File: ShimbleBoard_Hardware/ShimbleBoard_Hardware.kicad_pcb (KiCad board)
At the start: 2 copper layers, 13 parts, among them U1 TM4C129E_Launchpad, U2 OKI

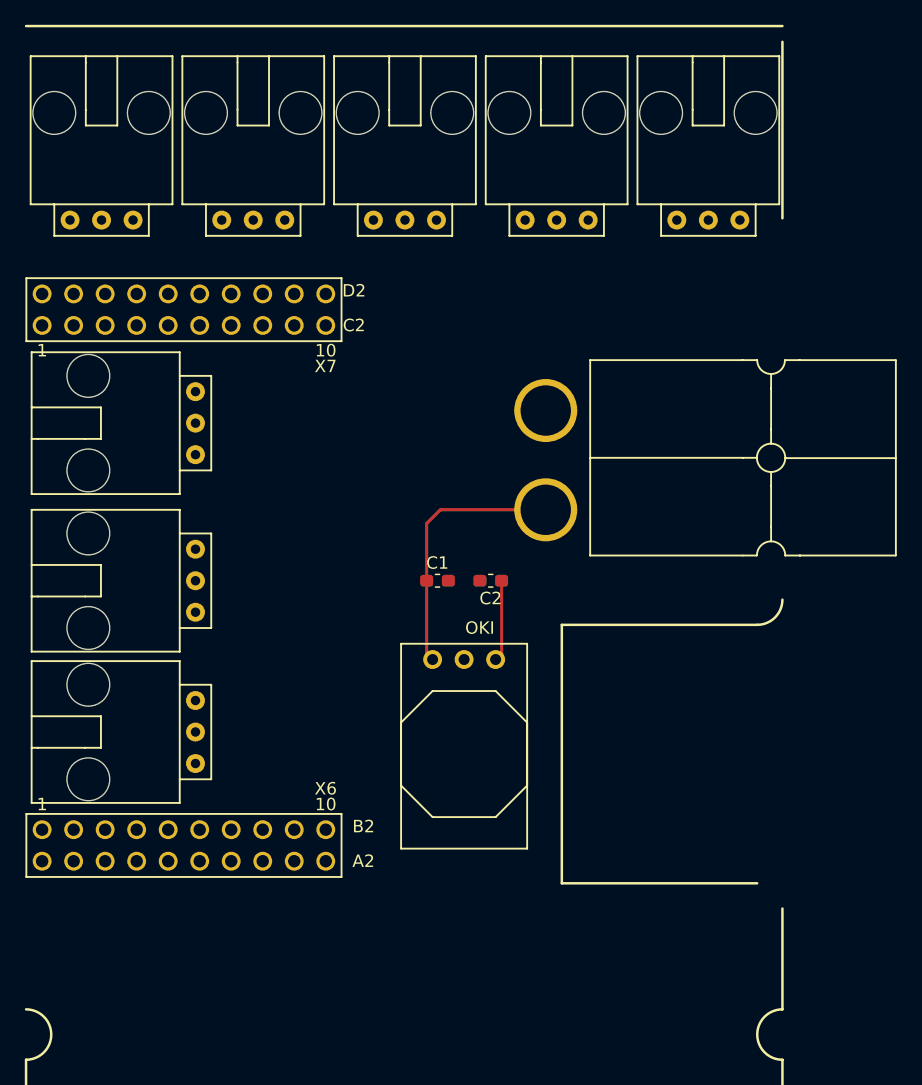
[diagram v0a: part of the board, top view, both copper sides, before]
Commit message: Removed Servo 8 & Increased Power Track Width
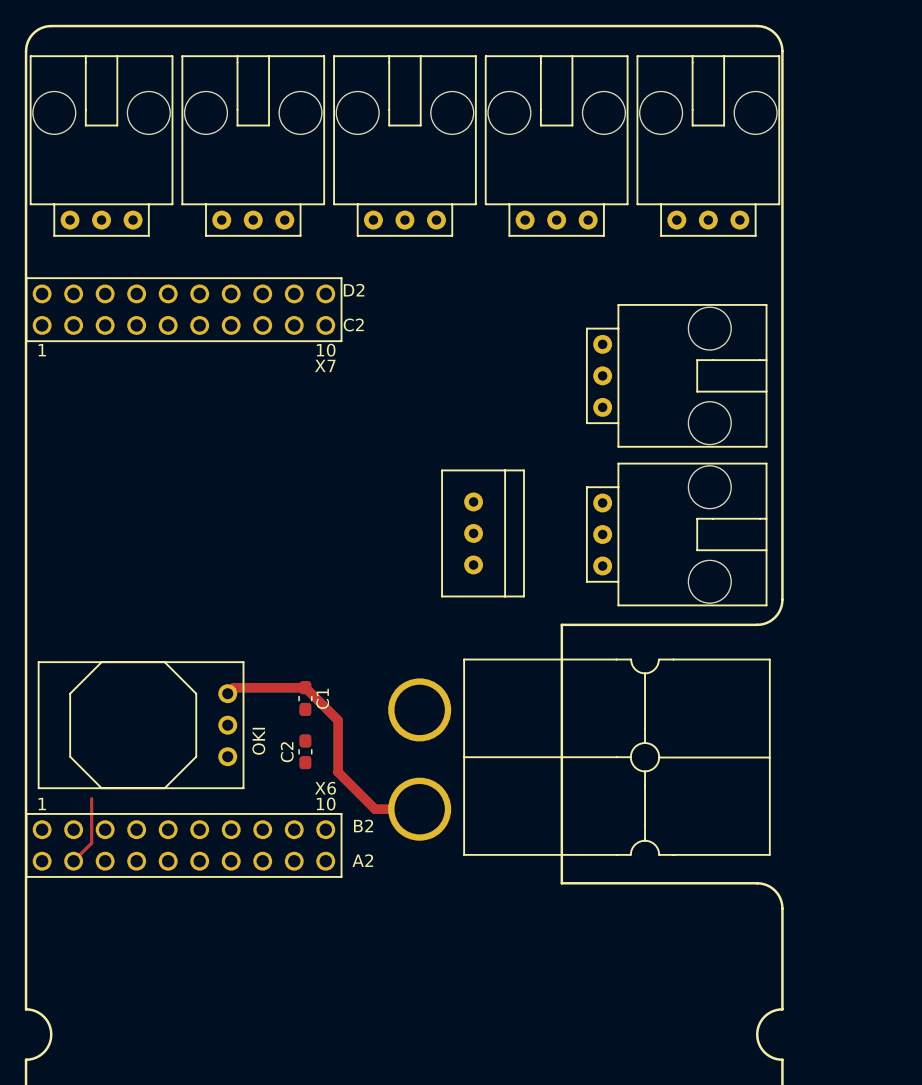
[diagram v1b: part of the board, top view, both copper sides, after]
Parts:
- Conn9: footprint MRDT_Connectors:MOLEX_SL_03_Horizontal -> MRDT_Connectors:MOLEX_SL_03_Vertical
- moved Conn7 43.6 mm to (139.4, 87.6), turned to 270 degrees
- moved Conn8 33.0 mm to (139.4, 100.4), turned to 270 degrees
- moved Conn1 26.2 mm to (128.3, 110.5)
- moved Conn9 25.2 mm to (131.6, 95.2), turned to 270 degrees
- moved C2 20.3 mm to (115.5, 117.9), turned to 90 degrees
- moved C1 14.3 mm to (115.5, 113.6), turned to 270 degrees
- moved U2 12.8 mm to (110.5, 110.7), turned to 270 degrees
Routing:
- net +5V: track 6.55 -> 0.00 mm
- net Servo_6_Ctrl: track 0.00 -> 5.63 mm
- net Net-(C1-Pad1): track 21.2 -> 22.2 mm

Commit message: Board Review
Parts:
- added G***: LOGO, MRDT_Silkscreens:MRDT_Logo_20mm, F.Cu at (105.9, 140.2)
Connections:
- U1 pad PA4: Servo_7_Ctrl -> Net-(U1-PadPA4)
- U1 pad PA5: Servo_8_Ctrl -> Net-(U1-PadPA5)
- U1 pad PA7: Net-(U1-PadPA7) -> Servo_2_Ctrl
- U1 pad PD2: Servo_6_Ctrl -> Net-(U1-PadPD2)
- U1 pad PG1: Servo_1_Ctrl -> Servo_8_Ctrl
- U1 pad PK4: Servo_2_Ctrl -> Servo_7_Ctrl
- U1 pad PK5: Servo_3_Ctrl -> Servo_6_Ctrl
- U1 pad PM0: Servo_4_Ctrl -> Servo_5_Ctrl
- U1 pad PM1: Net-(U1-PadPM1) -> Servo_4_Ctrl
- U1 pad PM6: Net-(U1-PadPM6) -> Servo_3_Ctrl
- U1 pad PM7: Servo_5_Ctrl -> Servo_1_Ctrl
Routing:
- net Servo_7_Ctrl: track 0.00 -> 58.3 mm
- net Servo_5_Ctrl: track 0.00 -> 57.9 mm
- net Servo_8_Ctrl: track 0.00 -> 50.7 mm
- net Servo_4_Ctrl: track 0.00 -> 42.1 mm
- net Servo_6_Ctrl: track 5.63 -> 43.1 mm
- net Servo_2_Ctrl: track 0.00 -> 14.9 mm
- net Servo_3_Ctrl: track 0.00 -> 12.3 mm
- net Servo_1_Ctrl: track 0.00 -> 7.78 mm
- net +5V: track 0.00 -> 6.46 mm
- added copper zone on B.Cu, net +5V
- added copper zone on F.Cu, net GND
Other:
- board text added: "ShimbleBoard_Hardware, Rev. 1 Mars Rover Design Team, 2019 Missouri S&T Andrew Phillips"

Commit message: Revised Schematic
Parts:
- added C3: 10uF, Capacitor_SMD:C_0603_1608Metric_Pad1.05x0.95mm_HandSolder, F.Cu at (61.3, 88.9)
- added C4: 10uF, Capacitor_SMD:C_0603_1608Metric_Pad1.05x0.95mm_HandSolder, F.Cu at (38.2, 98.8)
- added D1: D_Schottky, Diode_SMD:D_0603_1608Metric_Pad1.05x0.95mm_HandSolder, F.Cu at (60.5, 71.4)
- added D10: Ctrl_6_LED, Diode_SMD:D_0603_1608Metric_Pad1.05x0.95mm_HandSolder, F.Cu at (77.2, 172.7)
- added D11: Ctrl_7_LED, Diode_SMD:D_0603_1608Metric_Pad1.05x0.95mm_HandSolder, F.Cu at (77.2, 177.0)
- added D12: Ctrl_8_LED, Diode_SMD:D_0603_1608Metric_Pad1.05x0.95mm_HandSolder, F.Cu at (77.2, 181.4)
- added D2: D_Schottky, Diode_SMD:D_0603_1608Metric_Pad1.05x0.95mm_HandSolder, F.Cu at (38.2, 88.1)
- added D3: 5V_Act_LED, Diode_SMD:D_0603_1608Metric_Pad1.05x0.95mm_HandSolder, F.Cu at (77.6, 142.2)
- added D4: 5V_Log_LED, Diode_SMD:D_0603_1608Metric_Pad1.05x0.95mm_HandSolder, F.Cu at (77.6, 146.6)
- added D5: Ctrl_1_LED, Diode_SMD:D_0603_1608Metric_Pad1.05x0.95mm_HandSolder, F.Cu at (77.6, 150.9)
- added D6: Ctrl_2_LED, Diode_SMD:D_0603_1608Metric_Pad1.05x0.95mm_HandSolder, F.Cu at (77.6, 155.4)
- added D7: Ctrl_3_LED, Diode_SMD:D_0603_1608Metric_Pad1.05x0.95mm_HandSolder, F.Cu at (92.6, 159.5)
- added D8: Ctrl_4_LED, Diode_SMD:D_0603_1608Metric_Pad1.05x0.95mm_HandSolder, F.Cu at (77.4, 164.1)
- added D9: Ctrl_5_LED, Diode_SMD:D_0603_1608Metric_Pad1.05x0.95mm_HandSolder, F.Cu at (96.2, 166.1)
- added L1: 47uH, Inductor_SMD:L_0603_1608Metric_Pad1.05x0.95mm_HandSolder, F.Cu at (57.8, 78.0)
- added L2: 47uH, Diode_SMD:D_0603_1608Metric_Pad1.05x0.95mm_HandSolder, F.Cu at (37.3, 93.5)
- added R1: 500, Resistor_SMD:R_0603_1608Metric_Pad1.05x0.95mm_HandSolder, F.Cu at (72.0, 142.2)
- added R10: 500, Resistor_SMD:R_0603_1608Metric_Pad1.05x0.95mm_HandSolder, F.Cu at (72.0, 181.4)
- added R2: 500, Resistor_SMD:R_0603_1608Metric_Pad1.05x0.95mm_HandSolder, F.Cu at (72.0, 146.6)
- added R3: 500, Resistor_SMD:R_0603_1608Metric_Pad1.05x0.95mm_HandSolder, F.Cu at (72.0, 150.9)
- added R4: 500, Resistor_SMD:R_0603_1608Metric_Pad1.05x0.95mm_HandSolder, F.Cu at (72.0, 155.4)
- added R5: 500, Resistor_SMD:R_0603_1608Metric_Pad1.05x0.95mm_HandSolder, F.Cu at (72.0, 159.8)
- added R6: 500, Resistor_SMD:R_0603_1608Metric_Pad1.05x0.95mm_HandSolder, F.Cu at (72.0, 164.1)
- added R7: 500, Resistor_SMD:R_0603_1608Metric_Pad1.05x0.95mm_HandSolder, F.Cu at (72.0, 168.4)
- added R8: 500, Resistor_SMD:R_0603_1608Metric_Pad1.05x0.95mm_HandSolder, F.Cu at (72.0, 172.7)
- added R9: 500, Resistor_SMD:R_0603_1608Metric_Pad1.05x0.95mm_HandSolder, F.Cu at (72.0, 177.0)
- added U3: AP1059, Package_SO:SOIC-8_3.9x4.9mm_P1.27mm, F.Cu at (45.7, 93.5)
- Conn1: footprint MRDT_Connectors:Anderson_2_Horisontal_Side_by_Side -> MRDT_Connectors:Anderson_3_Horisontal_Side_by_Side
- U2: value OKI -> AP1059; footprint MRDT_Devices:OKI_Horizontal -> Package_SO:SOIC-8_3.9x4.9mm_P1.27mm
- moved U2 53.1 mm to (68.1, 78.7), turned to 0 degrees
- moved Conn9 48.6 mm to (176.8, 77.5)
- moved Conn1 5.43 mm to (129.3, 105.2)
- moved Conn8 2.84 mm to (140.7, 97.9)
- moved Conn7 2.84 mm to (140.7, 85.1)
- moved C2 2.76 mm to (114.0, 115.6), turned to 0 degrees
- moved C1 2.51 mm to (117.4, 112.0), turned to 0 degrees
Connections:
- net Net-(C1-Pad1) renamed V+Log
- C2 pad 1: +5V -> GND
- C2 pad 2: GND -> V+Act
- Conn2 pad 1: +5V -> +5VA
- Conn3 pad 1: +5V -> +5VA
- Conn4 pad 1: +5V -> +5VA
- Conn5 pad 1: +5V -> +5VA
- Conn6 pad 1: +5V -> +5VA
- Conn7 pad 1: +5V -> +5VA
- Conn8 pad 1: +5V -> +5VA
- Conn9 pad 1: +5V -> +5VA
- U1 pad +5V: +5V -> +5VL
- U2 pad 2: GND -> Net-(D1-Pad1)
- U2 pad 3: +5V -> +5VL
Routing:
- net Servo_5_Ctrl: track 57.9 -> 0.00 mm
- net Servo_7_Ctrl: track 58.3 -> 24.7 mm
- net Servo_8_Ctrl: track 50.7 -> 27.8 mm
- net V+Log: track 22.2 -> 0.00 mm
- net Servo_6_Ctrl: track 43.1 -> 21.6 mm
- net +5V: track 6.46 -> 0.00 mm
- added copper zone on B.Cu, net +5VL
- removed copper zone on B.Cu, net +5V

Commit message: Work hours 2018-11-17
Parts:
- moved D12 87.2 mm to (114.3, 102.5)
- moved R10 87.2 mm to (109.1, 102.5)
- moved D11 86.0 mm to (114.3, 99.4)
- moved R9 86.0 mm to (109.1, 99.4)
- moved D10 84.9 mm to (114.3, 96.4)
- moved R8 84.9 mm to (109.1, 96.4)
- moved R7 83.9 mm to (109.1, 93.1)
- moved D9 75.2 mm to (114.3, 93.1)
- moved D1 73.5 mm to (115.2, 120.4), turned to 180 degrees
- moved L1 70.5 mm to (116.9, 116.4), turned to 180 degrees
- moved R5 67.0 mm to (98.9, 98.4)
- moved D8 66.9 mm to (104.0, 102.7)
- moved R6 66.9 mm to (98.7, 102.7)
- moved R4 65.7 mm to (98.9, 95.5)
- moved D6 65.5 mm to (104.0, 95.5)
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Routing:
- net Servo_5_Ctrl: track 0.00 -> 57.7 mm
- net GND: track 0.00 -> 56.8 mm
- net +5VL: track 0.00 -> 39.6 mm
- net V+Act: track 0.00 -> 38.5 mm, vias 0 -> 2
- net Servo_7_Ctrl: track 24.7 -> 56.4 mm
- net Servo_6_Ctrl: track 21.6 -> 44.6 mm
- net Servo_8_Ctrl: track 27.8 -> 49.9 mm
- net V+Log: track 0.00 -> 14.9 mm, vias 0 -> 2
- net +5VA: track 0.00 -> 11.1 mm
- net Servo_3_Ctrl: track 12.3 -> 22.5 mm
- net Servo_2_Ctrl: track 14.9 -> 22.0 mm
- net Net-(D1-Pad1): track 0.00 -> 6.98 mm
- net Net-(D2-Pad1): track 0.00 -> 6.97 mm
- net Servo_1_Ctrl: track 7.78 -> 11.3 mm
- net Net-(D7-Pad2): track 0.00 -> 3.33 mm
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- removed copper zone on B.Cu, net +5VL
- removed copper zone on F.Cu, net GND
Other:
- board text added: "Orange"

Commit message: Preliminary traces completed & Various review changes
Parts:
- moved D4 34.1 mm to (120.7, 104.9)
- moved R2 33.6 mm to (114.6, 104.9)
- moved D3 24.1 mm to (107.3, 104.9)
- moved R1 23.7 mm to (101.2, 104.9)
- moved D12 6.37 mm to (120.7, 102.0)
- moved D11 6.36 mm to (120.7, 99.1)
- moved D9 6.36 mm to (120.7, 93.3)
- moved D10 6.35 mm to (120.7, 96.2)
- moved R9 5.48 mm to (114.6, 99.1)
- moved R10 5.47 mm to (114.6, 102.0)
- moved R7 5.45 mm to (114.6, 93.3)
- moved R8 5.45 mm to (114.6, 96.2)
- moved D5 3.41 mm to (107.3, 93.4)
- moved D6 3.40 mm to (107.3, 96.3)
- moved D7 3.37 mm to (107.3, 99.2)
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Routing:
- net +5VA: track 11.1 -> 107.4 mm, vias 0 -> 3
- net GND: track 56.8 -> 99.4 mm, vias 0 -> 2
- net +5VL: track 39.6 -> 70.4 mm
- net Servo_4_Ctrl: track 42.3 -> 69.5 mm, vias 0 -> 2
- net Servo_3_Ctrl: track 22.5 -> 48.7 mm, vias 0 -> 1
- net Servo_8_Ctrl: track 49.9 -> 64.7 mm
- net Servo_7_Ctrl: track 56.4 -> 68.9 mm, vias 0 -> 2
- net Servo_1_Ctrl: track 11.3 -> 23.8 mm, vias 0 -> 1
- net Servo_2_Ctrl: track 22.0 -> 33.7 mm, vias 0 -> 1
- net Servo_6_Ctrl: track 44.6 -> 56.2 mm, vias 0 -> 2
- net Servo_5_Ctrl: track 57.7 -> 66.4 mm, vias 0 -> 2
- net Net-(D12-Pad2): track 0.00 -> 4.35 mm
- net Net-(D10-Pad2): track 0.00 -> 4.35 mm
- net Net-(D4-Pad2): track 0.00 -> 4.35 mm
- net Net-(D9-Pad2): track 0.00 -> 4.35 mm
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- added copper zone on F.Cu, net +5VA
- added copper zone on B.Cu, net GND
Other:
- board text added: "+5VA"
- board text added: "+5VL"
- board text added: "Indicators"
- board text added: "Servo 1"
- board text added: "Servo 2"
- board text added: "Servo 3"
- board text added: "Servo 4"
- board text added: "Servo 5"
- board text added: "Servo 6"
- board text added: "Servo 7"
- board text added: "Servo 8"
- board text added: "Shimble Board, Rev. 1, 2019 Mars Rover Design Team Missouri S&T Andrew Phillips"
- board text removed: "Orange"
- board text removed: "ShimbleBoard_Hardware, Rev. 1 Mars Rover Design Team, 2019 Missouri S&T Andrew Phillips"

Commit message: Eh?
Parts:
- removed the C2 at (117.0, 108.2)
- added C2: 10uF, Capacitor_SMD:C_0603_1608Metric_Pad1.05x0.95mm_HandSolder, F.Cu at (62.4, 103.9)
- added C2: 10uF, Capacitor_SMD:C_0603_1608Metric_Pad1.05x0.95mm_HandSolder, F.Cu at (75.4, 103.6)
- added C4: 10uF, Capacitor_SMD:C_0603_1608Metric_Pad1.05x0.95mm_HandSolder, F.Cu at (58.9, 110.5)
- added D2: D_Schottky, Diode_SMD:D_0603_1608Metric_Pad1.05x0.95mm_HandSolder, F.Cu at (59.8, 105.0)
- added G***: LOGO, ShimbleBoard_Hardware:Andrew_Phillips_Sig_19.7mmx7.7mm, F.Cu at (134.6, 146.1)
- added L2: 47uH, Diode_SMD:D_0603_1608Metric_Pad1.05x0.95mm_HandSolder, F.Cu at (58.9, 108.0)
- added U3: AP1059, Package_SO:SOIC-8_3.9x4.9mm_P1.27mm, F.Cu at (65.0, 108.6)
- moved D2 24.7 mm to (72.9, 104.8), turned to 90 degrees
- moved C4 24.6 mm to (72.0, 110.2)
- moved U3 24.5 mm to (78.1, 108.3)
- moved L2 24.1 mm to (72.0, 107.7)
- moved C1 10.4 mm to (112.3, 119.4), turned to 180 degrees
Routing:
- net GND: track 99.4 -> 75.7 mm, vias 2 -> 5
- net V+Act: track 38.5 -> 49.2 mm, vias 2 -> 1
- net Net-(D2-Pad1): track 6.97 -> 0.00 mm
- net +5VA: track 107.4 -> 106.9 mm, vias 3 -> 2
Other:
- board outline added: 157.7 x 154.6 mm

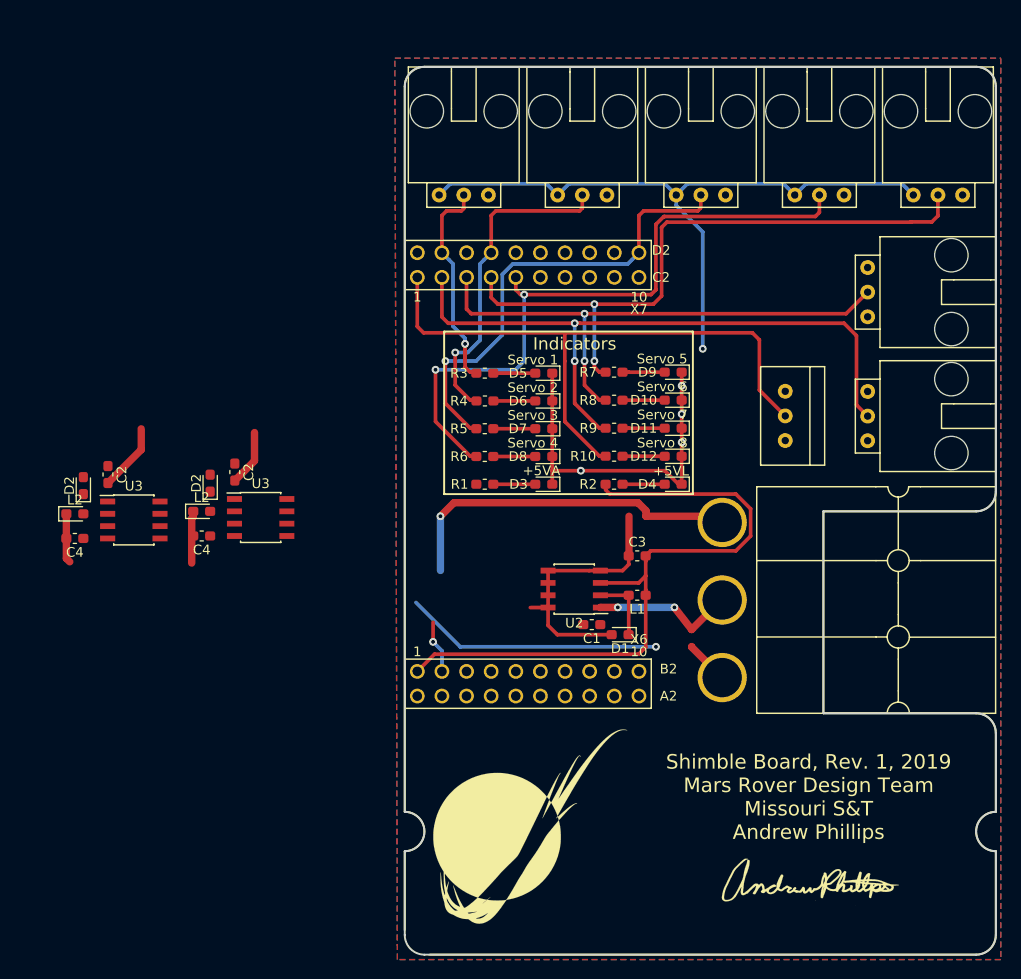
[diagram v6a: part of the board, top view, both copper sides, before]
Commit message: BOM and Redesigned AP1509 Area
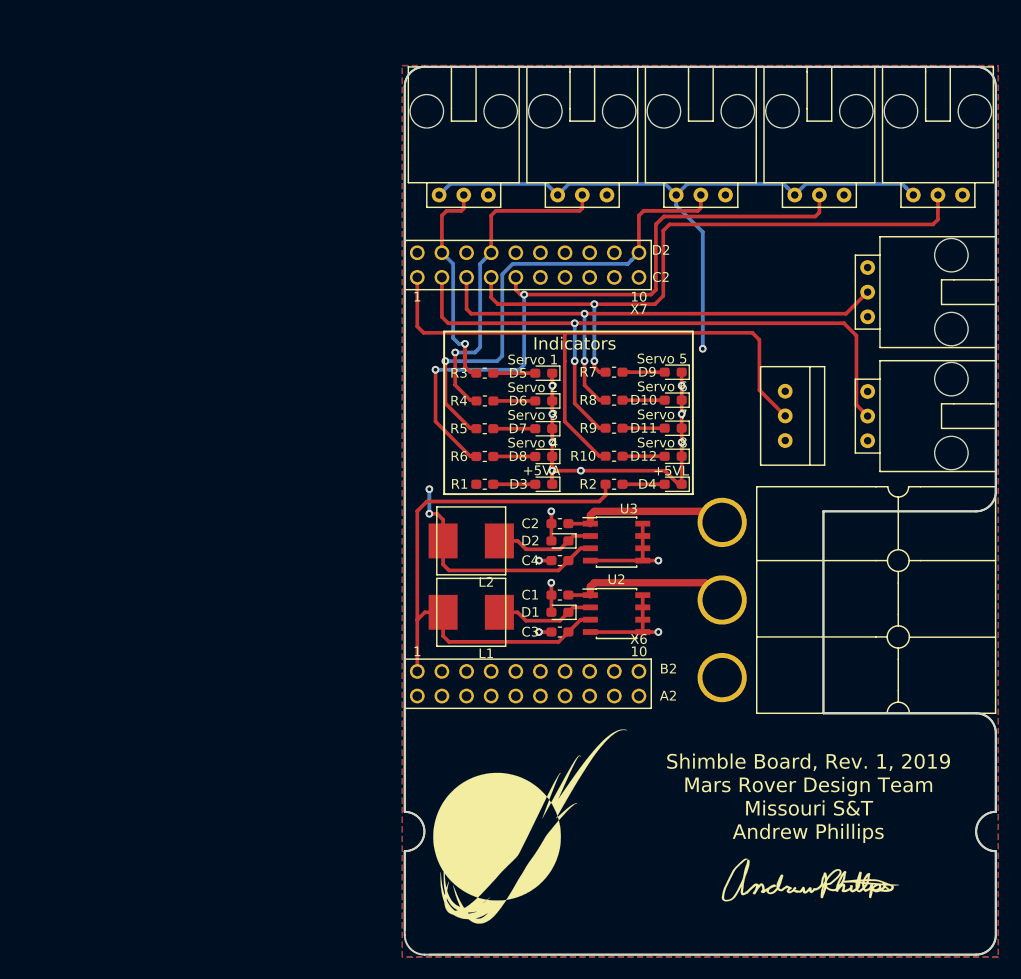
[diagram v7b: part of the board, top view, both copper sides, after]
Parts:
- removed the C2 at (75.4, 103.6)
- removed the C4 at (72.0, 110.2)
- removed the D2 at (72.9, 104.8)
- removed the L2 at (72.0, 107.7)
- removed the U3 at (78.1, 108.3)
- L1: footprint Inductor_SMD:L_0603_1608Metric_Pad1.05x0.95mm_HandSolder -> ShimbleBoard_Hardware:ETQ-P4M470YFN_Inductor
- L2: footprint Diode_SMD:D_0603_1608Metric_Pad1.05x0.95mm_HandSolder -> ShimbleBoard_Hardware:ETQ-P4M470YFN_Inductor
- moved C4 50.1 mm to (109.0, 112.8), turned to 0 degrees
- moved U3 49.8 mm to (114.8, 110.9)
- moved D2 49.5 mm to (109.0, 110.7), turned to 180 degrees
- moved C2 46.9 mm to (109.0, 109.0), turned to 0 degrees
- moved L2 41.0 mm to (99.8, 110.7)
- moved L1 17.2 mm to (99.8, 118.1), turned to 0 degrees
- moved C3 11.2 mm to (109.0, 120.1)
- moved D1 6.62 mm to (109.0, 118.1)
- moved U2 5.04 mm to (114.8, 118.2), turned to 0 degrees
- moved C1 4.48 mm to (109.0, 116.3)
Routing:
- net V+Act: track 49.2 -> 18.3 mm, vias 1 -> 0
- net +5VA: track 106.9 -> 94.9 mm, vias 2 -> 3
- net +5VL: track 70.4 -> 59.6 mm
- net Net-(D2-Pad1): track 0.00 -> 10.3 mm
- net GND: track 75.7 -> 71.4 mm, vias 5 -> 14
- net Net-(D1-Pad1): track 6.98 -> 10.3 mm
- net V+Log: track 14.9 -> 17.7 mm, vias 2 -> 0
- net Servo_3_Ctrl: track 48.7 -> 49.9 mm

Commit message: PRR Take 1
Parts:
- moved C1 0.76 mm to (109.0, 117.1)
- moved C3 0.76 mm to (109.0, 120.9)
- moved D1 0.76 mm to (109.0, 118.9)
- moved L1 0.76 mm to (99.8, 118.9)
- moved U2 0.76 mm to (114.8, 119.0)
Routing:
- net +5VA: track 94.9 -> 82.9 mm, vias 3 -> 2
- net GND: track 71.4 -> 70.1 mm, vias 14 -> 13
- net Servo_5_Ctrl: track 66.4 -> 66.2 mm, vias 2 -> 3
- net (no net): vias 0 -> 5
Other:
- board size 157.7 x 154.6 mm -> 61 x 91.6 mm
